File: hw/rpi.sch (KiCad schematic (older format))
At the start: 0 parts

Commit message: hw: add CAT24C32 EEPROM symbol
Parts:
- added XP?: Rpi_40PIN, symbol Rpi_40PIN
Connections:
- new net +3.3VP: XP?.1 (3v3), XP?.17 (3v3)
- new net +5VP: XP?.2 (5v), XP?.4 (5v)
- new net GND: XP?.14 (GND), XP?.20 (GND), XP?.25 (GND), XP?.30 (GND), XP?.34 (GND), XP?.39 (GND), XP?.6 (GND), XP?.9 (GND)
- new net RPI_GPCLK0: XP?.7 (BCM4_GPCLK0)
- new net RPI_RX: XP?.~ (BCM15_RXD)
- new net RPI_SCL: XP?.5 (BCM3_SCL)
- new net RPI_SDA: XP?.3 (BCM2_SDA)
- new net RPI_TX: XP?.8 (BCM14_TXD)
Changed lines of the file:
@@
 LIBS:contrib
 LIBS:valves
+LIBS:rpi_con
+LIBS:obc-drone-hat-cache
 EELAYER 25 0
 EELAYER END
@@
 Comment4 ""
 $EndDescr
+$Comp
+L Rpi_40PIN XP?
+U 1 1 5AAFFE0B
+P 4100 3600
+F 0 "XP?" H 3550 4800 60  0000 C CNN
+F 1 "Rpi_40PIN" H 4150 2400 60  0000 C CNN
+F 2 "" H 3750 3700 60  0001 C CNN
+F 3 "" H 3750 3700 60  0001 C CNN
+	1    4100 3600
+	1    0    0    -1
+$EndComp
+$Comp
+L +3.3VP #PWR?
+U 1 1 5AAFFF4C
+P 3050 2400
+F 0 "#PWR?" H 3200 2350 50  0001 C CNN
+F 1 "+3.3VP" H 3050 2500 50  0000 C CNN
+F 2 "" H 3050 2400 50  0001 C CNN
+F 3 "" H 3050 2400 50  0001 C CNN
+	1    3050 2400
+	1    0    0    -1
+$EndComp
+$Comp
+L +5VP #PWR?
+U 1 1 5AAFFF63
+P 5200 2400
+F 0 "#PWR?" H 5200 2250 50  0001 C CNN
+F 1 "+5VP" H 5200 2540 50  0000 C CNN
+F 2 "" H 5200 2400 50  0001 C CNN
+F 3 "" H 5200 2400 50  0001 C CNN
+	1    5200 2400
+	1    0    0    -1
+$EndComp
+$Comp
+L GND #PWR?
+U 1 1 5AAFFFA2
+P 2950 4900
+F 0 "#PWR?" H 2950 4650 50  0001 C CNN
+F 1 "GND" H 2950 4750 50  0000 C CNN
+F 2 "" H 2950 4900 50  0001 C CNN
+F 3 "" H 2950 4900 50  0001 C CNN
+	1    2950 4900
+	1    0    0    -1
+$EndComp
+Wire Wire Line
+	3250 2650 3050 2650
+Wire Wire Line
+	3050 2400 3050 3450
+Wire Wire Line
+	3050 3450 3250 3450
+Connection ~ 3050 2650
+Wire Wire Line
+	3250 3050 2950 3050
+Wire Wire Line
+	2950 3050 2950 4900
+Wire Wire Line
+	3250 3850 2950 3850
+Connection ~ 2950 3850
+Wire Wire Line
+	3250 4550 2950 4550
+Connection ~ 2950 4550
+$Comp
+L GND #PWR?
+U 1 1 5AB000E4
+P 5300 4900
+F 0 "#PWR?" H 5300 4650 50  0001 C CNN
+F 1 "GND" H 5300 4750 50  0000 C CNN
+F 2 "" H 5300 4900 50  0001 C CNN
+F 3 "" H 5300 4900 50  0001 C CNN
+	1    5300 4900
+	1    0    0    -1
+$EndComp
+Wire Wire Line
+	4950 2750 5200 2750
+Wire Wire Line
+	5200 2750 5200 2400
+Wire Wire Line
+	4950 2650 5200 2650
+Connection ~ 5200 2650
+Wire Wire Line
+	4950 2850 5300 2850
+Wire Wire Line
+	5300 2850 5300 4900
+Wire Wire Line
+	4950 3250 5300 3250
+Connection ~ 5300 3250
+Wire Wire Line
+	4950 3550 5300 3550
+Connection ~ 5300 3550
+Wire Wire Line
+	4950 4050 5300 4050
+Connection ~ 5300 4050
+Wire Wire Line
+	4950 4250 5300 4250
+Connection ~ 5300 4250
+Text GLabel 5850 2950 2    60   Output ~ 0
+RPI_TX
+Text GLabel 5850 3050 2    60   Input ~ 0
+RPI_RX
+Wire Wire Line
+	4950 2950 5850 2950
+Wire Wire Line
+	4950 3050 5850 3050
+Text GLabel 2500 2950 0    60   Output ~ 0
+RPI_GPCLK0
+Text GLabel 2500 2850 0    60   BiDi ~ 0
+RPI_SCL
+Text GLabel 2500 2750 0    60   BiDi ~ 0
+RPI_SDA
+Wire Wire Line
+	2500 2750 3250 2750
+Wire Wire Line
+	2500 2850 3250 2850
+Wire Wire Line
+	2500 2950 3250 2950
 $EndSCHEMATC

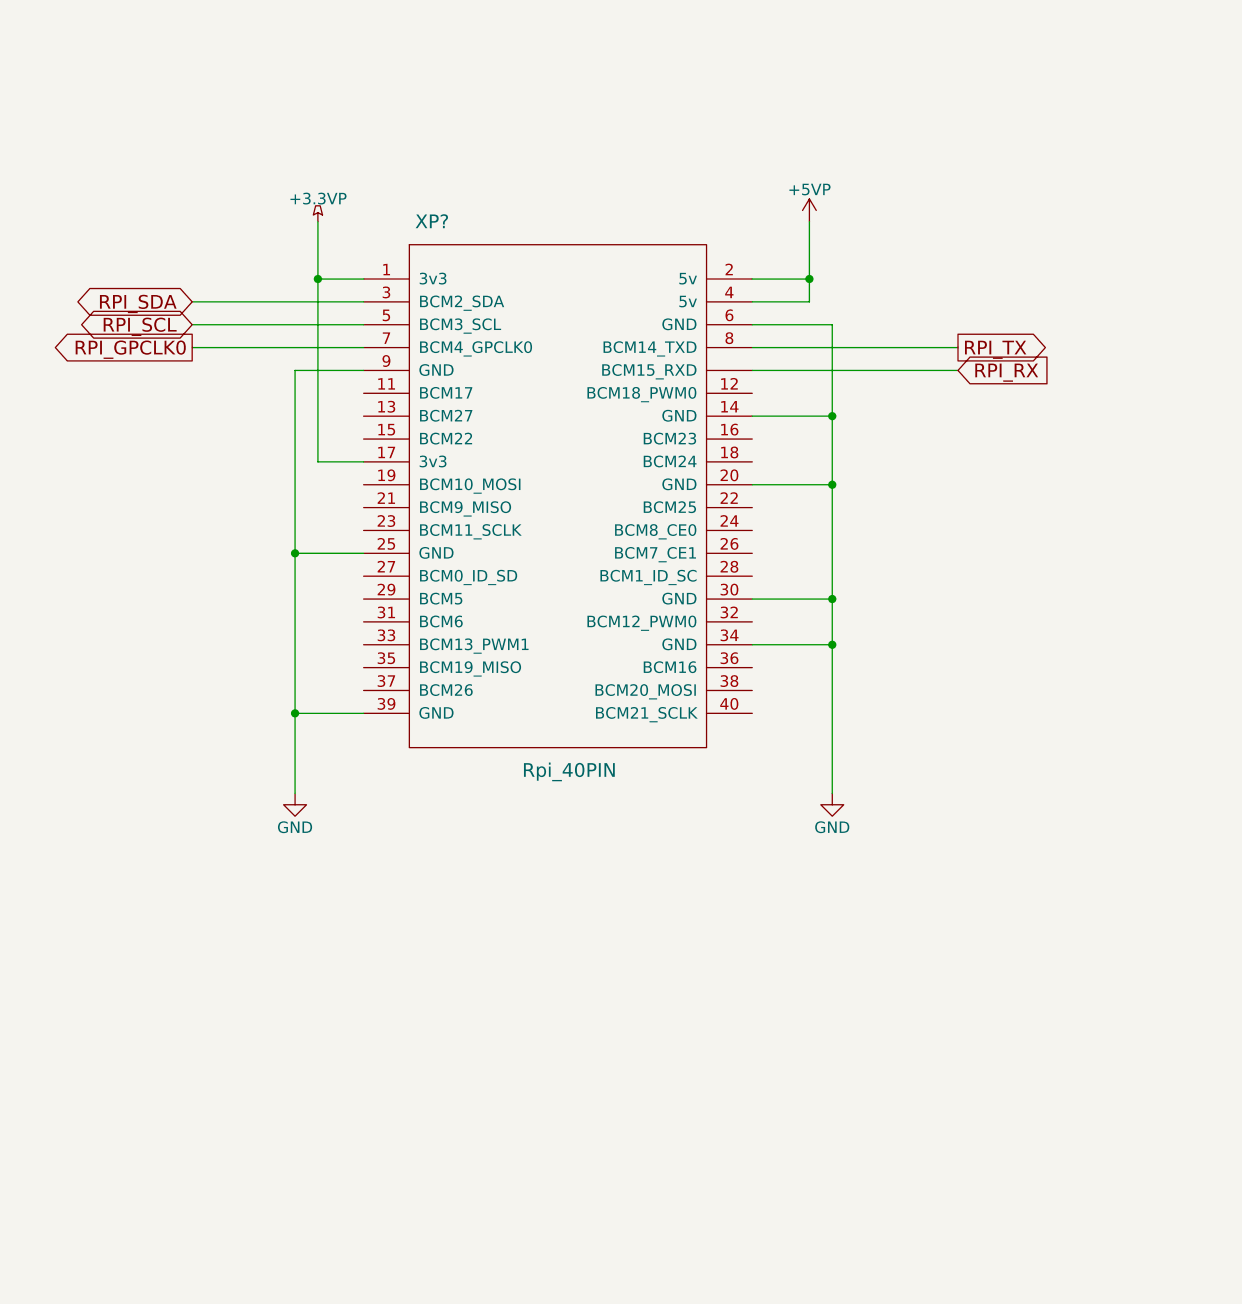
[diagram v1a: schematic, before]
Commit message: hw: select pins for serial interrupt and stm control
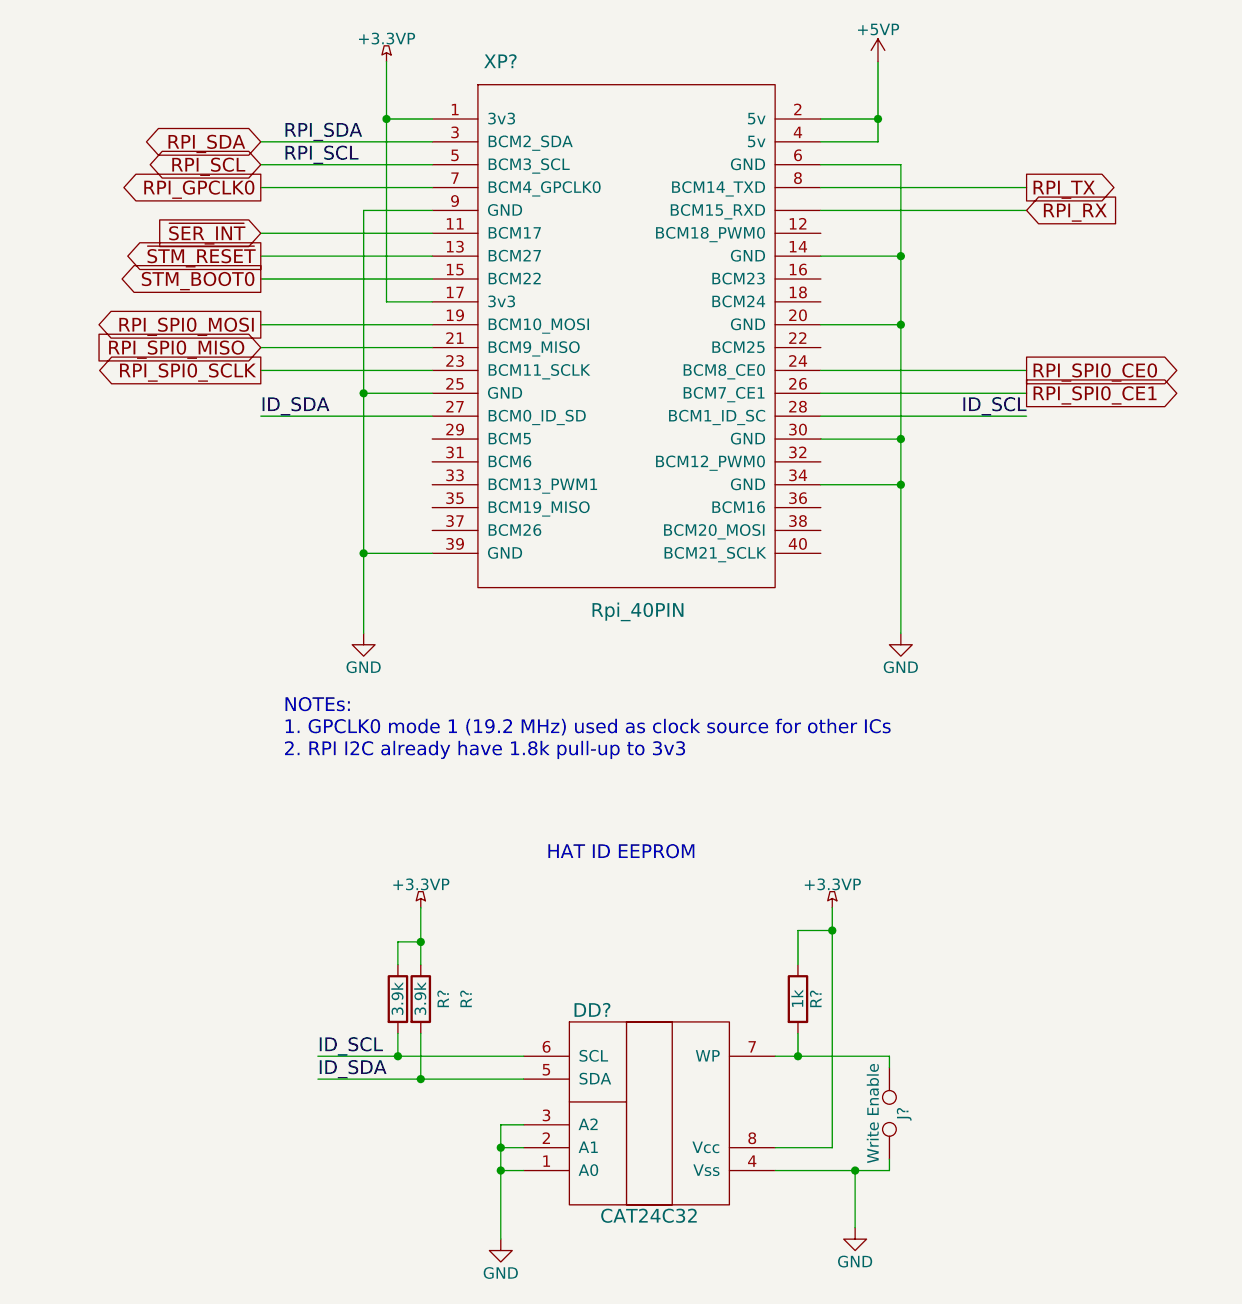
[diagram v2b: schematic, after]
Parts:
- added DD?: CAT24C32, symbol CAT24
- added J?: Write Enable, symbol TEST_2P
- added R?: 1k, symbol R
- added R? (x2): 3.9k, symbol R
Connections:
- net +3.3VP: now also DD?.8 (Vcc), R?.1, R?.1, R?.1
- net GND: now also DD?.1 (A0), DD?.2 (A1), DD?.3 (A2), DD?.4 (Vss), J?.2
- net ~SER_INT: now reaches XP?.11 (BCM17)
- net ~STM_RESET: now reaches XP?.13 (BCM27)
- net STM_BOOT0: now reaches XP?.15 (BCM22)
- net RPI_SPI0_MOSI: now reaches XP?.19 (BCM10_MOSI)
- net RPI_SPI0_MISO: now reaches XP?.21 (BCM9_MISO)
- net RPI_SPI0_SCLK: now reaches XP?.23 (BCM11_SCLK)
- net RPI_SPI0_CE0: now reaches XP?.24 (BCM8_CE0)
- net RPI_SPI0_CE1: now reaches XP?.26 (BCM7_CE1)
- net ID_SDA: now reaches XP?.27 (BCM0_ID_SD)
- net ID_SDA: now also DD?.5 (SDA), R?.2
- net ID_SCL: now reaches XP?.28 (BCM1_ID_SC)
- net ID_SCL: now also DD?.6 (SCL), R?.2
- new net: DD?.7 (WP), J?.1, R?.2
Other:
- note added: "HAT ID EEPROM"
- note added: "NOTEs:\n1. GPCLK0 mode 1 (19.2 MHz) used as clock source for other ICs\n2. RPI I2C already have 1.8k pull-up to 3v3"
- moved on the sheet: XP?
